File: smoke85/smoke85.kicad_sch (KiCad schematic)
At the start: 23 parts, among them J1 USB_C_Receptacle_USB2.0, J2 Conn_01x20, J3 Conn_01x20, U1 STM32F072CBT6, U2 PRTR5V0U2X, U3 XC6206PxxxMR-Regulator_Linear

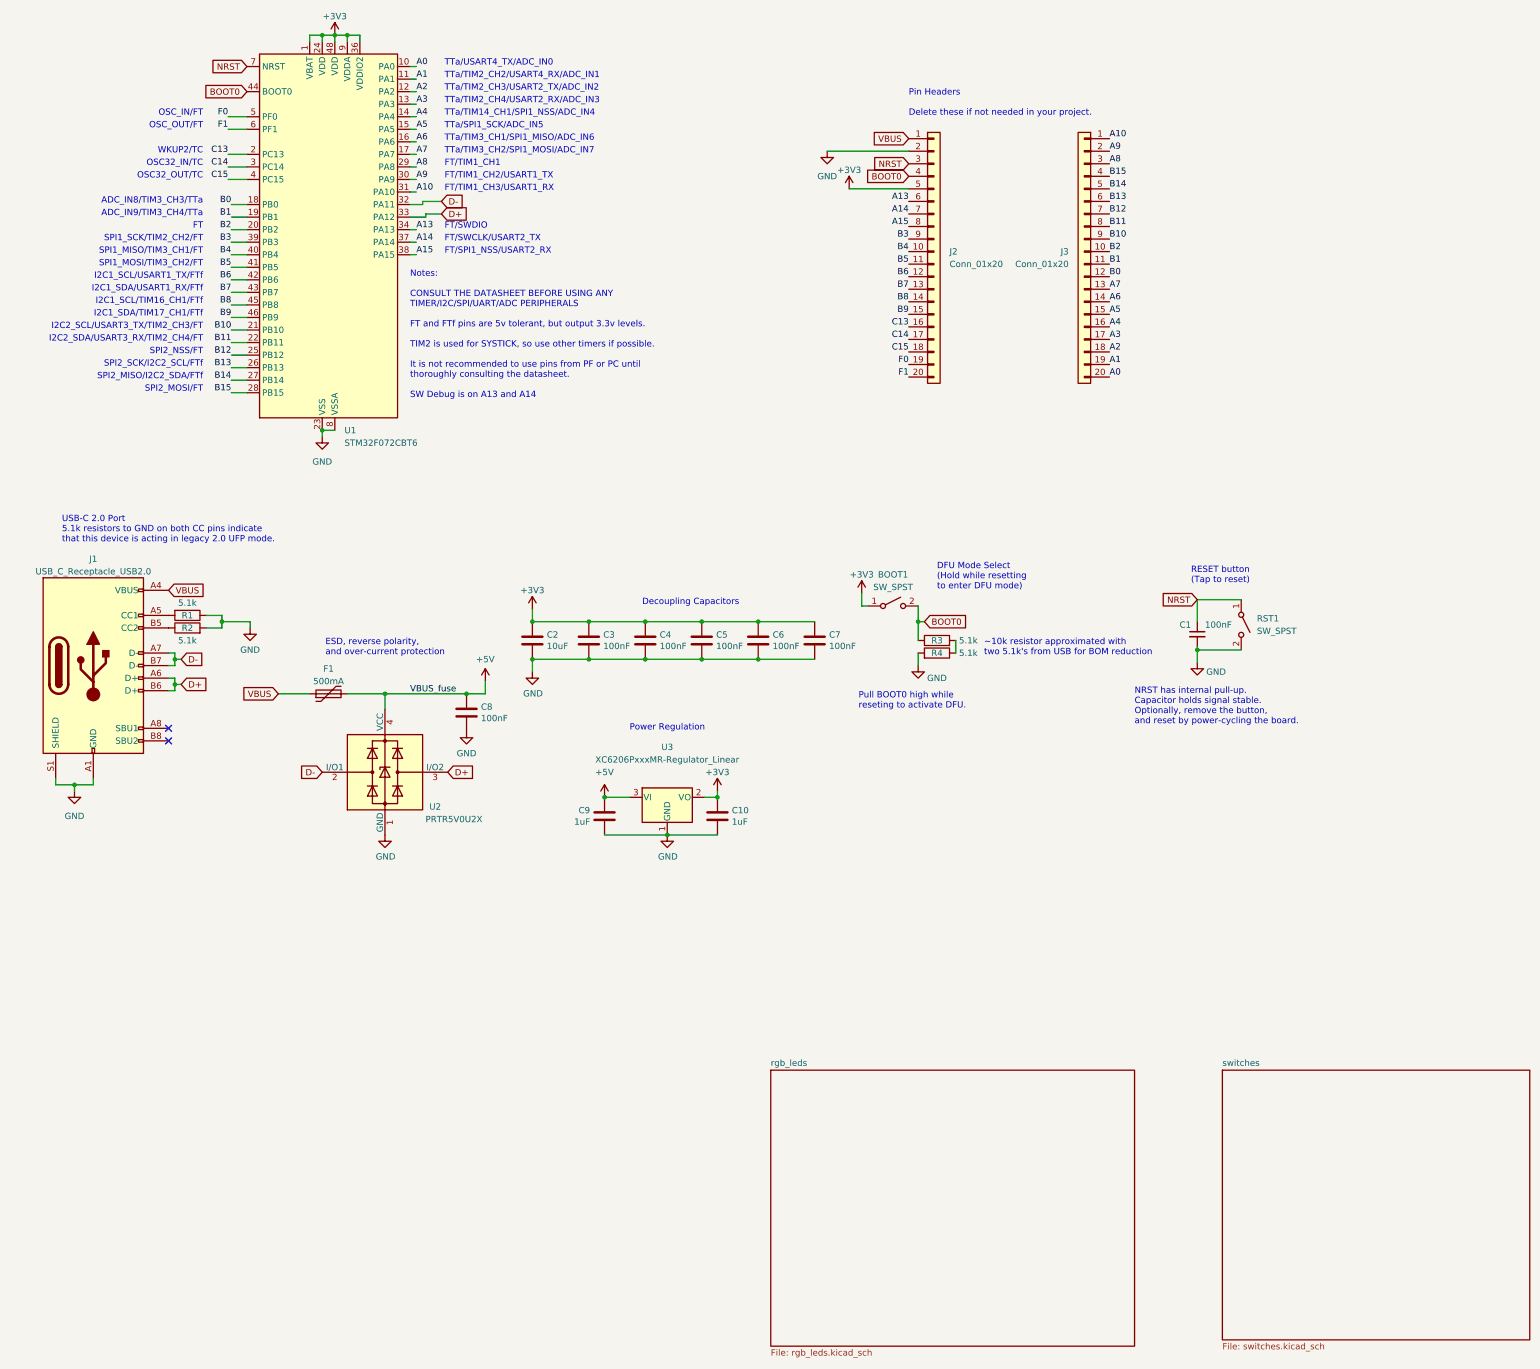
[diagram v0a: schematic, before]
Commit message: start connecting rgb leds
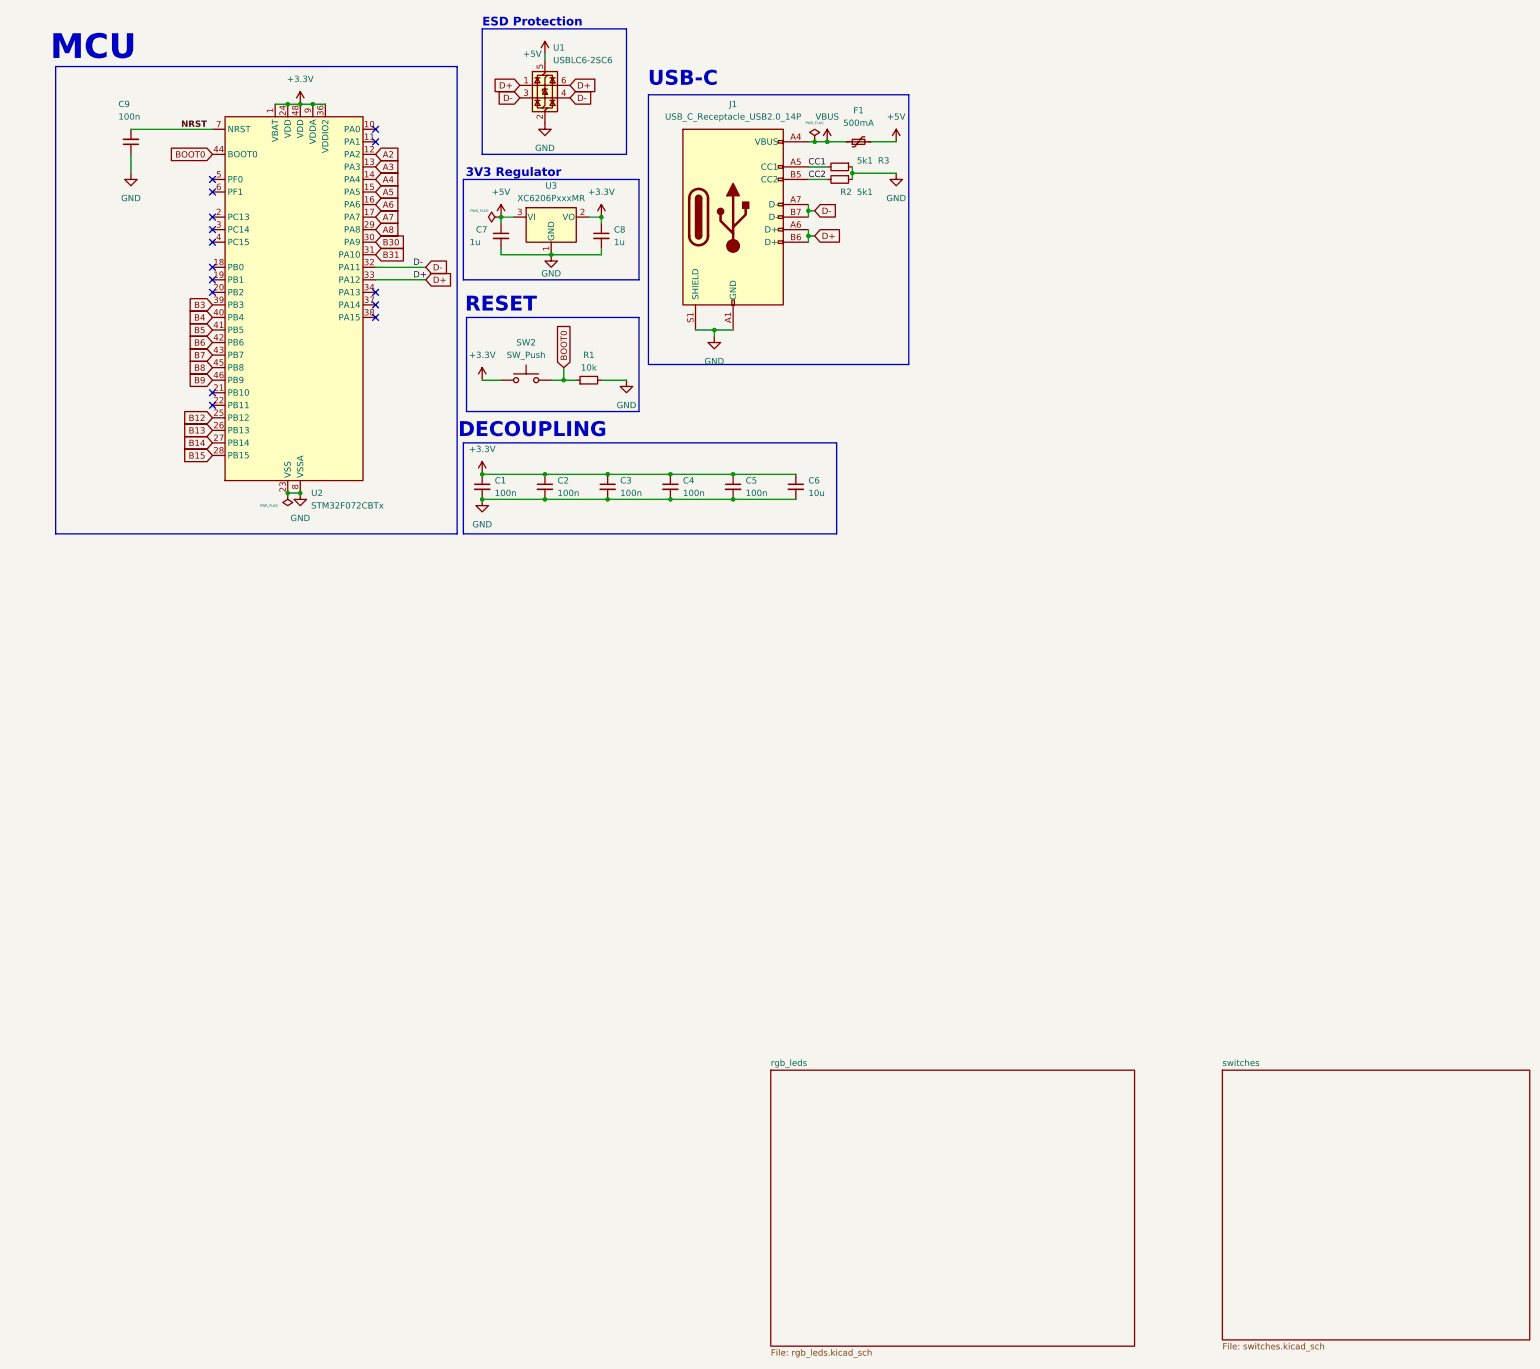
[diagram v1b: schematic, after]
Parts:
- removed BOOT1, RST1: SW_SPST, Button_Switch_SMD:SW_SPST_TL3342, symbol Switch:SW_SPST
- removed C10, C9: 1uF, Capacitor_SMD:C_0402_1005Metric, symbol Device:C
- removed C2: 10uF, Capacitor_SMD:C_0603_1608Metric, symbol Device:C
- removed C3, C4, C5, C6, C7, C8: 100nF, Capacitor_SMD:C_0402_1005Metric, symbol Device:C
- removed F1: 500mA, Fuse:Fuse_1206_3216Metric, symbol Device:Polyfuse
- removed J1: USB_C_Receptacle_USB2.0, Connector_USB:USB_C_Receptacle_HRO_TYPE-C-31-M-12, symbol Connector:USB_C_Receptacle_USB2.0
- removed J2, J3: Conn_01x20, Connector_PinHeader_2.54mm:PinHeader_1x20_P2.54mm_Vertical, symbol Connector_Generic:Conn_01x20
- removed R1, R2, R3, R4: 5.1k, Resistor_SMD:R_0402_1005Metric, symbol Device:R
- removed U1: STM32F072CBT6, Package_QFP:LQFP-48_7x7mm_P0.5mm, symbol MCU_ST_STM32F0:STM32F072CBTx
- removed U2: PRTR5V0U2X, Package_TO_SOT_SMD:SOT-143, symbol Power_Protection:PRTR5V0U2X
- removed U3: XC6206PxxxMR-Regulator_Linear, Package_TO_SOT_SMD:SOT-23, symbol kicad-keyboard-parts:XC6206PxxxMR-Regulator_Linear
- added C2, C3, C4, C5, C9: 100n, Capacitor_SMD:C_0805_2012Metric_Pad1.18x1.45mm_HandSolder, symbol Device:C_Small
- added C6: 10u, Capacitor_SMD:C_0805_2012Metric_Pad1.18x1.45mm_HandSolder, symbol Device:C_Small
- added C7, C8: 1u, Capacitor_SMD:C_0805_2012Metric_Pad1.18x1.45mm_HandSolder, symbol Device:C_Small
- added F1: 500mA, Fuse:Fuse_1206_3216Metric_Pad1.42x1.75mm_HandSolder, symbol Device:Polyfuse_Small
- added J1: USB_C_Receptacle_USB2.0_14P, Connector_USB:USB_C_Receptacle_HRO_TYPE-C-31-M-12, symbol Connector:USB_C_Receptacle_USB2.0_14P
- added R1: 10k, Resistor_SMD:R_0603_1608Metric_Pad0.98x0.95mm_HandSolder, symbol Device:R_Small
- added R2, R3: 5k1, Resistor_SMD:R_0603_1608Metric_Pad0.98x0.95mm_HandSolder, symbol Device:R_Small
- added SW2: SW_Push, Button_Switch_SMD:SW_SPST_TL3342, symbol Switch:SW_Push
- added U1: USBLC6-2SC6, Package_TO_SOT_SMD:SOT-23-6, symbol Power_Protection:USBLC6-2SC6
- added U2: STM32F072CBTx, Package_QFP:LQFP-48_7x7mm_P0.5mm, symbol MCU_ST_STM32F0:STM32F072CBTx
- added U3: XC6206PxxxMR, Package_TO_SOT_SMD:SOT-23-3, symbol Regulator_Linear:XC6206PxxxMR
- C1: value 100nF -> 100n; footprint Capacitor_SMD:C_0402_1005Metric -> Capacitor_SMD:C_0805_2012Metric_Pad1.18x1.45mm_HandSolder; LCSC C307331 -> (none)
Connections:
- net +5V: now also C7.1, F1.2, U1.5 (VBUS), U3.3 (VI)
- net A2: now also U2.12 (PA2)
- net A3: now also U2.13 (PA3)
- net A4: now also U2.14 (PA4)
- net A5: now also U2.15 (PA5)
- net A6: now also U2.16 (PA6)
- net A7: now also U2.17 (PA7)
- net A8: now also U2.29 (PA8)
- net B12: now also U2.25 (PB12)
- net B13: now also U2.26 (PB13)
- net B14: now also U2.27 (PB14)
- net B15: now also U2.28 (PB15)
- net B3: now also U2.39 (PB3)
- net B4: now also U2.40 (PB4)
- net B5: now also U2.41 (PB5)
- net B6: now also U2.42 (PB6)
- net B7: now also U2.43 (PB7)
- net B8: now also U2.45 (PB8)
- net B9: now also U2.46 (PB9)
- net BOOT0: now also R1.1, SW2.2, U2.44 (BOOT0)
- net D+: now also J1.A6 (D+), J1.B6 (D+), U1.1 (I/O1), U1.6 (I/O1), U2.33 (PA12)
- net D-: now also J1.A7 (D-), J1.B7 (D-), U1.3 (I/O2), U1.4 (I/O2), U2.32 (PA11)
- net GND: now also C2.2, C3.2, C4.2, C5.2, C6.2, C7.2, C8.2, C9.1, J1.A1 (GND), J1.A12 (GND), J1.B1 (GND), J1.B12 (GND), J1.S1 (SHIELD), R1.2, R2.1, R3.1, U1.2 (GND), U2.23 (VSS), U2.35 (VSS), U2.47 (VSS), U2.8 (VSSA), U3.1 (GND)
- net NRST: now also C9.2, U2.7 (NRST); no longer C1.1
- net VBUS: now also F1.1, J1.A4 (VBUS), J1.A9 (VBUS), J1.B4 (VBUS), J1.B9 (VBUS)
- new net +3.3V: C1.1, C2.1, C3.1, C4.1, C5.1, C6.1, C8.1, SW2.1, U2.1 (VBAT), U2.24 (VDD), U2.36 (VDDIO2), U2.48 (VDD), U2.9 (VDDA), U3.2 (VO)
- new net B30: U2.30 (PA9)
- new net B31: U2.31 (PA10)
- new net CC1: J1.A5 (CC1), R3.2
- new net CC2: J1.B5 (CC2), R2.2
- no-connect marks 2 -> 15
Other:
- note added: "3V3 Regulator"
- note added: "DECOUPLING"
- note added: "ESD Protection"
- note added: "MCU"
- note added: "RESET"
- note added: "USB-C"
- note removed: "ADC_IN8/TIM3_CH3/TTa"
- note removed: "ADC_IN9/TIM3_CH4/TTa"
- note removed: "DFU Mode Select (Hold while resetting to enter DFU mode)"
- note removed: "Decoupling Capacitors"
- note removed: "ESD, reverse polarity, and over-current protection"
- note removed: "FT"
- note removed: "FT/SPI1_NSS/USART2_RX"
- note removed: "FT/SWCLK/USART2_TX"
- note removed: "FT/SWDIO"
- note removed: "FT/TIM1_CH1"
- note removed: "FT/TIM1_CH2/USART1_TX"
- note removed: "FT/TIM1_CH3/USART1_RX"
- note removed: "I2C1_SCL/TIM16_CH1/FTf"
- note removed: "I2C1_SCL/USART1_TX/FTf"
- note removed: "I2C1_SDA/TIM17_CH1/FTf"
- note removed: "I2C1_SDA/USART1_RX/FTf"
- note removed: "I2C2_SCL/USART3_TX/TIM2_CH3/FT"
- note removed: "I2C2_SDA/USART3_RX/TIM2_CH4/FT"
- note removed: "NRST has internal pull-up. Capacitor holds signal stable. Optionally, remove the button, and reset by power-cycling the board."
- note removed: "Notes: CONSULT THE DATASHEET BEFORE USING ANY TIMER/I2C/SPI/UART/ADC PERIPHERALS FT and FTf pins are 5v tolerant, but output 3.3v levels. TIM2 is used for SYSTICK, so use other timers if possible. It is not recommended to use pins from PF or PC until thoroughly consulting the datasheet. SW Debug is on A13 and A14"
- note removed: "OSC32_IN/TC"
- note removed: "OSC32_OUT/TC"
- note removed: "OSC_IN/FT"
- note removed: "OSC_OUT/FT"
- note removed: "Pin Headers Delete these if not needed in your project."
- note removed: "Power Regulation"
- note removed: "Pull BOOT0 high while reseting to activate DFU."
- note removed: "RESET button (Tap to reset)"
- note removed: "SPI1_MISO/TIM3_CH1/FT"
- note removed: "SPI1_MOSI/TIM3_CH2/FT"
- note removed: "SPI1_SCK/TIM2_CH2/FT"
- note removed: "SPI2_MISO/I2C2_SDA/FTf"
- note removed: "SPI2_MOSI/FT"
- note removed: "SPI2_NSS/FT"
- note removed: "SPI2_SCK/I2C2_SCL/FTf"
- note removed: "TTa/SPI1_SCK/ADC_IN5"
- note removed: "TTa/TIM14_CH1/SPI1_NSS/ADC_IN4"
- note removed: "TTa/TIM2_CH2/USART4_RX/ADC_IN1"
- note removed: "TTa/TIM2_CH3/USART2_TX/ADC_IN2"
- note removed: "TTa/TIM2_CH4/USART2_RX/ADC_IN3"
- note removed: "TTa/TIM3_CH1/SPI1_MISO/ADC_IN6"
- note removed: "TTa/TIM3_CH2/SPI1_MOSI/ADC_IN7"
- note removed: "TTa/USART4_TX/ADC_IN0"
- note removed: "USB-C 2.0 Port 5.1k resistors to GND on both CC pins indicate that this device is acting in legacy 2.0 UFP mode."
- note removed: "WKUP2/TC"
- note removed: "~10k resistor approximated with two 5.1k's from USB for BOM reduction"
